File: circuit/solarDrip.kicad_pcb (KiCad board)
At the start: 2 copper layers, 57 x 50 mm, 41 parts, among them J1 solar_charger, J2 batt, J3 solar, J4 pump, J5 soil, J6 water, J7 USB_C_Receptacle_USB2.0_14P, J8 i2c, Q1 2N7002K, Q2 2N7002K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

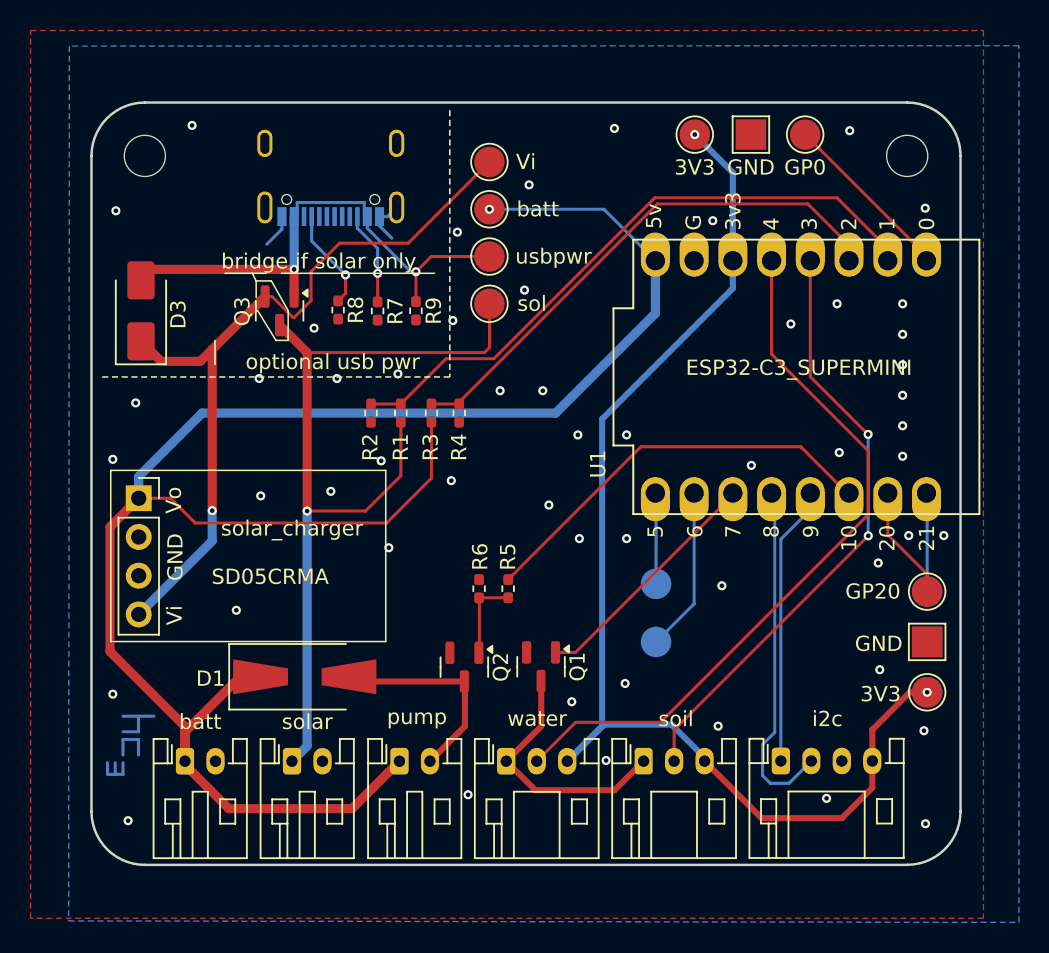
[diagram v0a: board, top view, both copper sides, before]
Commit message: flip usb and testpoint sides
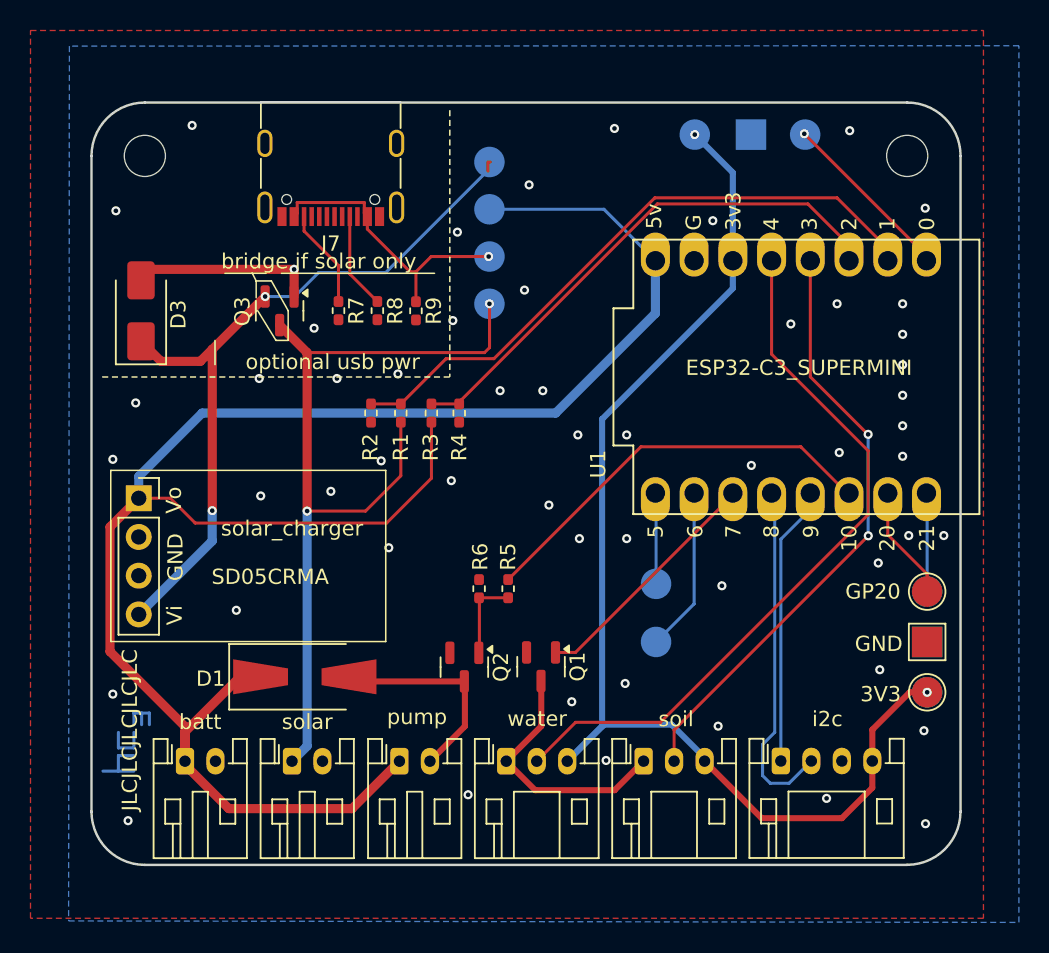
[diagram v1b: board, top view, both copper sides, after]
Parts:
- J7: moved to F.Cu
- TP1, TP10, TP15, TP2, TP3, TP6, TP7: moved to B.Cu
- moved REF** 4.92 mm to (21.5, 82.3), turned to 90 degrees
- moved R8 2.58 mm to (39.5, 52.1)
- moved R7 2.57 mm to (37.0, 52.1)
- turned J7 to 180 degrees
- turned TP1 to 180 degrees
- turned TP10 to 180 degrees
- turned TP15 to 180 degrees
- turned TP2 to 180 degrees
- turned TP3 to 180 degrees
- turned TP6 to 180 degrees
- turned TP7 to 180 degrees
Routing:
- net GND: track 5.36 -> 0.00 mm
- net vcc_usb: track 34.3 -> 30.9 mm
- net vcc_pwr: track 51.0 -> 49.1 mm, vias 1 -> 2
- net Net-(J7-CC2): track 6.15 -> 6.51 mm, vias 1 -> 0
- net Net-(J7-CC1): track 6.66 -> 6.32 mm, vias 1 -> 0
- net vcc_solar: track 55.4 -> 55.5 mm, vias 1 -> 2
- net gpio0: track 11.6 -> 11.7 mm, vias 0 -> 1
- net vcc_battery: vias 1 -> 0

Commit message: add capacitor, cleanup
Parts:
- removed REF**: muccc_logo, my_footprints:muccc_logo
- added C1: C_Polarized, Capacitor_THT:CP_Radial_D10.0mm_P7.50mm, F.Cu at (46.0, 71.0)
- moved R6 9.35 mm to (49.5, 61.6)
- moved R5 9.29 mm to (51.3, 61.6)
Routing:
- net vcc_battery: track 125.6 -> 138.9 mm
- net vcc_solar: track 55.5 -> 66.4 mm
- net Net-(Q2-G): track 5.54 -> 15.5 mm
- net out_pump: track 27.2 -> 20.4 mm
- net vcc_usb: track 30.9 -> 36.2 mm
- net out_sensors: track 16.0 -> 19.6 mm
- net GND: track 0.00 -> 2.74 mm, vias 54 -> 57
- net vcc_pwr: track 49.1 -> 51.7 mm
- net in-a_moisture: track 39.7 -> 42.2 mm
- net in-a_water: track 47.7 -> 49.6 mm
- net vcc_logic: vias 2 -> 1

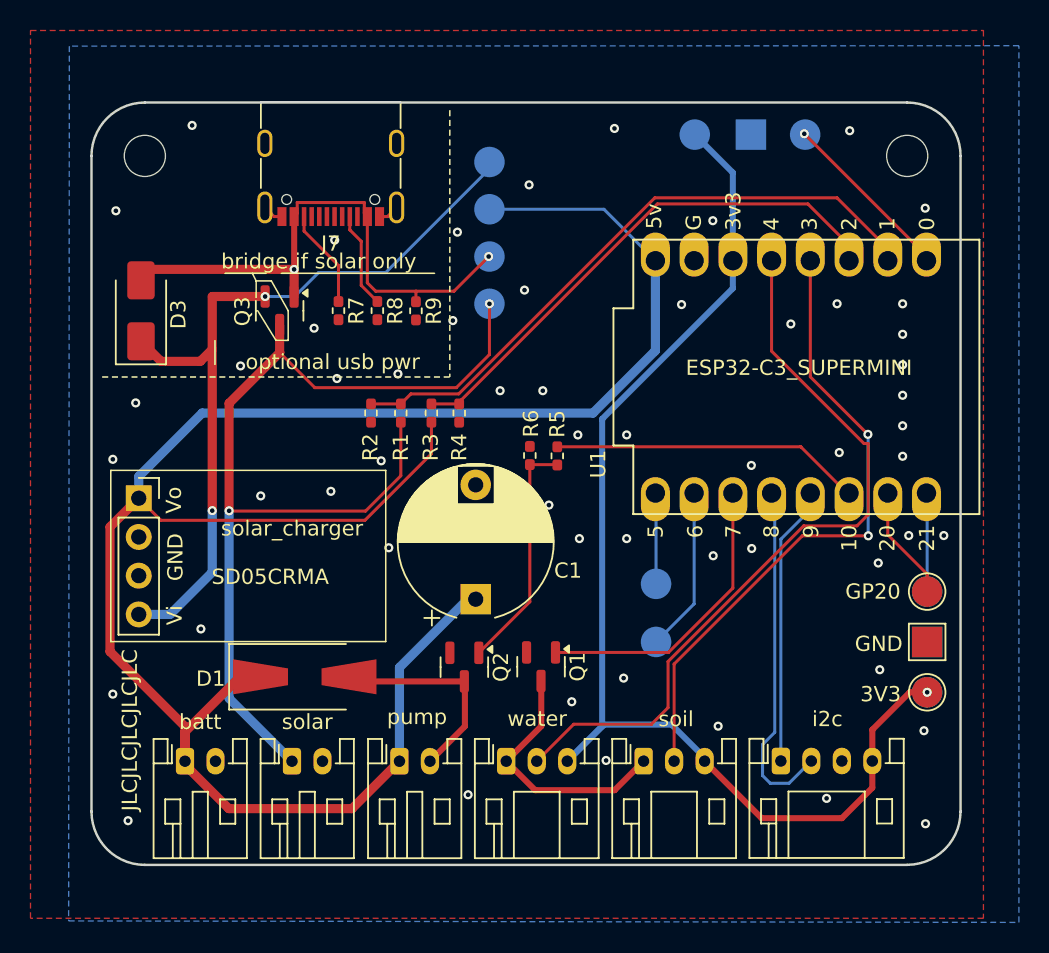
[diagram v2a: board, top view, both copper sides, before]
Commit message: move usb_pwr parts around
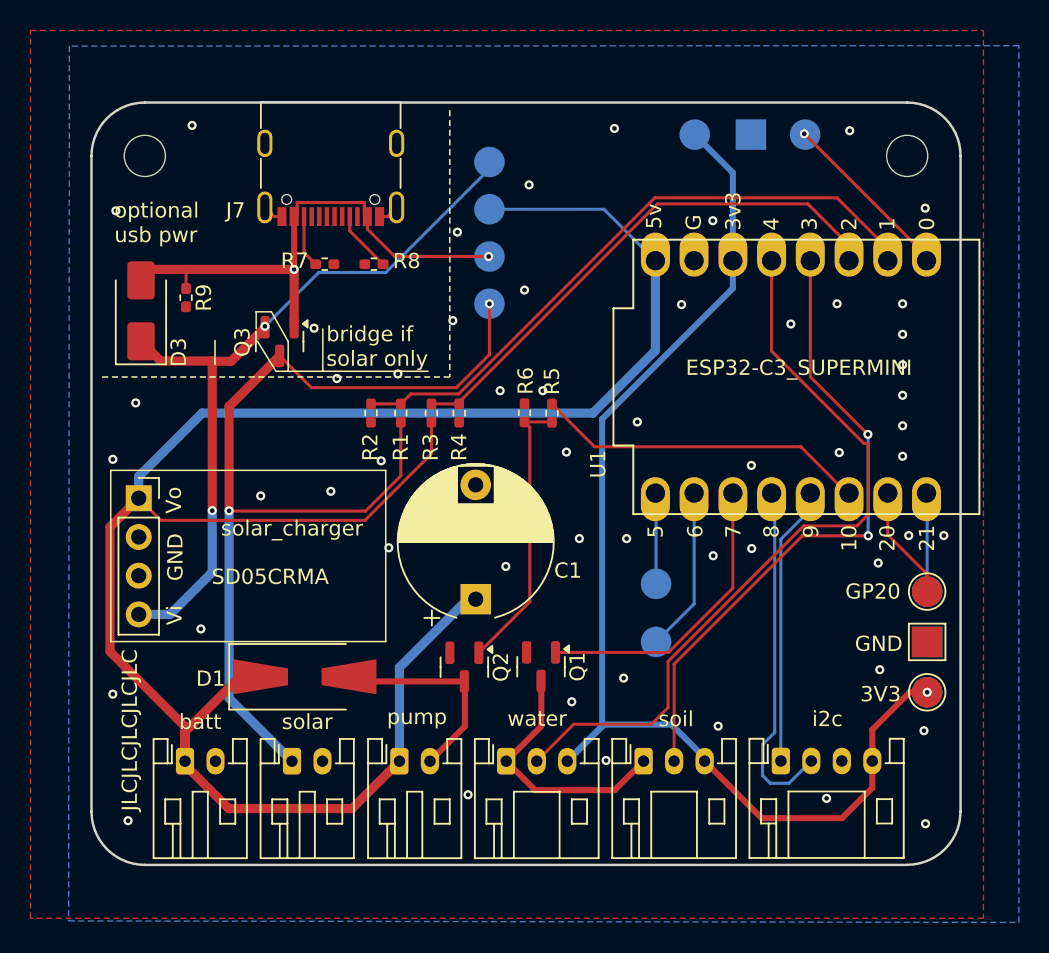
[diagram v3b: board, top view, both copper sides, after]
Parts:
- moved R9 15.1 mm to (26.9, 51.3)
- moved R7 3.18 mm to (36.0, 49.1), turned to 0 degrees
- moved R8 3.06 mm to (39.3, 49.1), turned to 180 degrees
- moved R6 2.82 mm to (49.1, 58.8)
- moved R5 2.82 mm to (51.0, 58.9)
- moved Q3 2.02 mm to (33.1, 54.1)
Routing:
- net Net-(J7-CC2): track 6.51 -> 3.43 mm
- net Net-(Q2-G): track 15.5 -> 18.5 mm
- net vcc_pwr: track 51.7 -> 48.9 mm
- net Net-(J7-CC1): track 6.32 -> 4.02 mm
- net vcc_solar: track 66.4 -> 64.3 mm
- net out_pump: track 20.4 -> 21.9 mm
- net vcc_usb: track 36.2 -> 34.9 mm
- net GND: vias 57 -> 55
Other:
- board text added: "SolarDripIrrigation v0.1 9R 05/2024"
- board text removed: "SolarDripIrigation v0.1 9R 05/2024"

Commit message: move more stuff around
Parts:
- C1: footprint Capacitor_THT:CP_Radial_D10.0mm_P7.50mm -> Capacitor_THT:CP_Radial_D8.0mm_P3.80mm
- moved J1 8.45 mm to (31.8, 61.4), turned to -90 degrees
- moved D1 4.54 mm to (37.0, 72.2), turned to -90 degrees
- moved C1 3.58 mm to (44.5, 67.8), turned to 0 degrees
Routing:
- net vcc_battery: track 138.9 -> 97.2 mm, vias 0 -> 2
- net vcc_pwr: track 48.9 -> 35.5 mm, vias 2 -> 1
- net vcc_solar: track 64.3 -> 51.5 mm, vias 2 -> 1
- net pump_low: track 13.9 -> 15.7 mm
- net GND: vias 55 -> 54
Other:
- board text added: "JLCJLCJLCJLC"
- board text removed: "JLCJLCJLCJLCJLC"

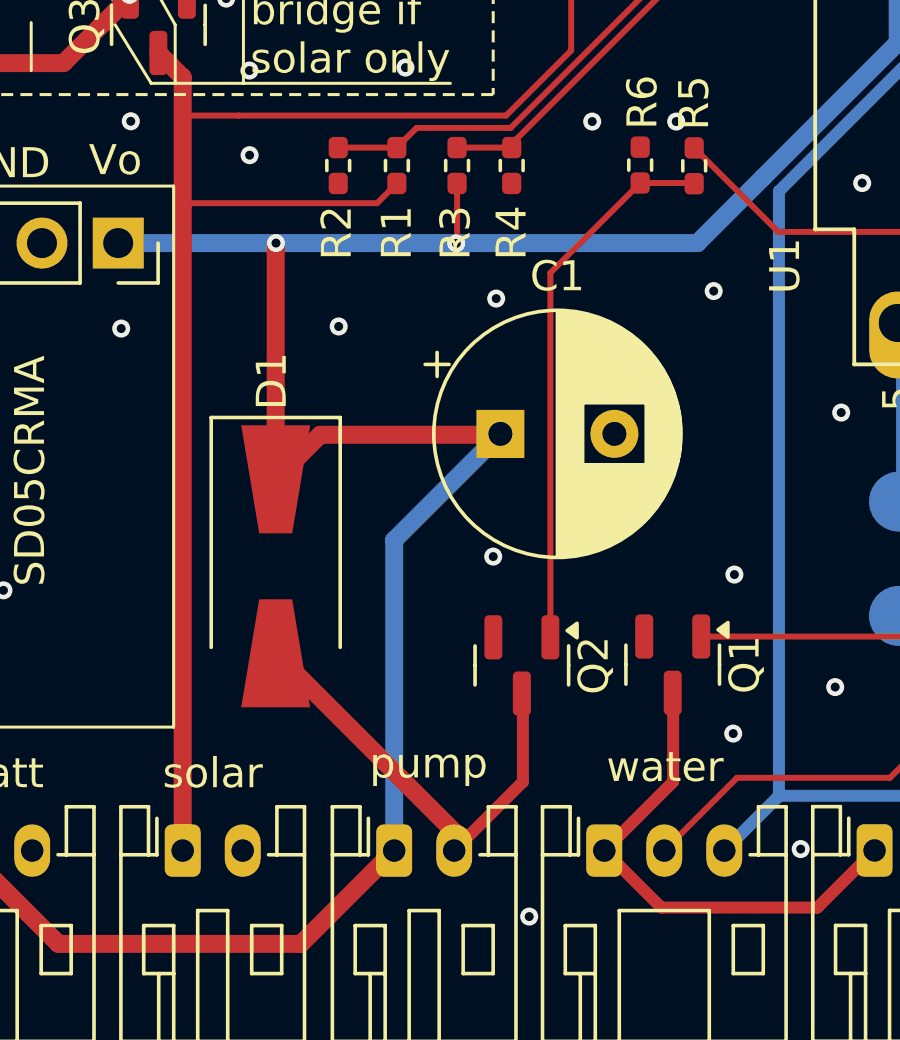
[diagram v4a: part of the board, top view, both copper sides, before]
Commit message: add motor cap
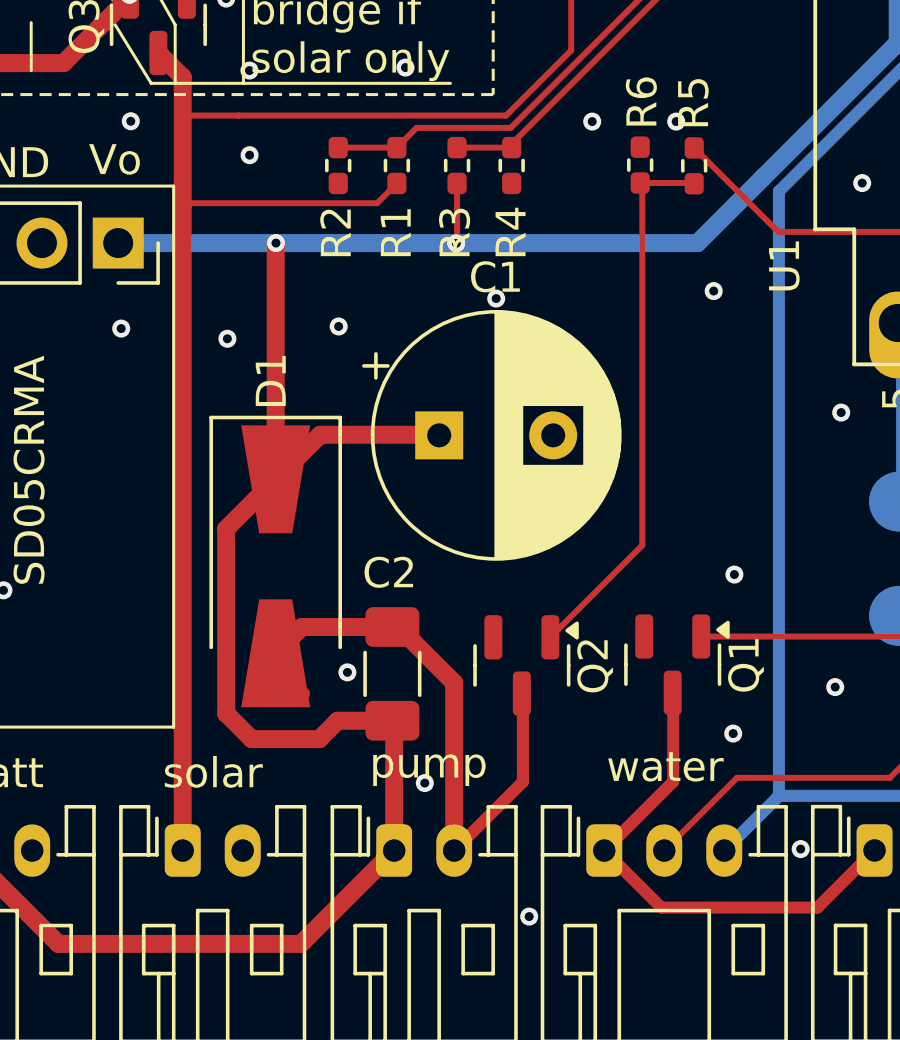
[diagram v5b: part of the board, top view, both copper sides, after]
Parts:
- added C2: C, Capacitor_SMD:C_1206_3216Metric_Pad1.33x1.80mm_HandSolder, F.Cu at (40.9, 75.8)
- moved C1 2.04 mm to (42.5, 67.8)
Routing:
- net pump_low: track 15.7 -> 19.4 mm
- net vcc_battery: track 97.2 -> 98.8 mm
- net GND: vias 54 -> 56

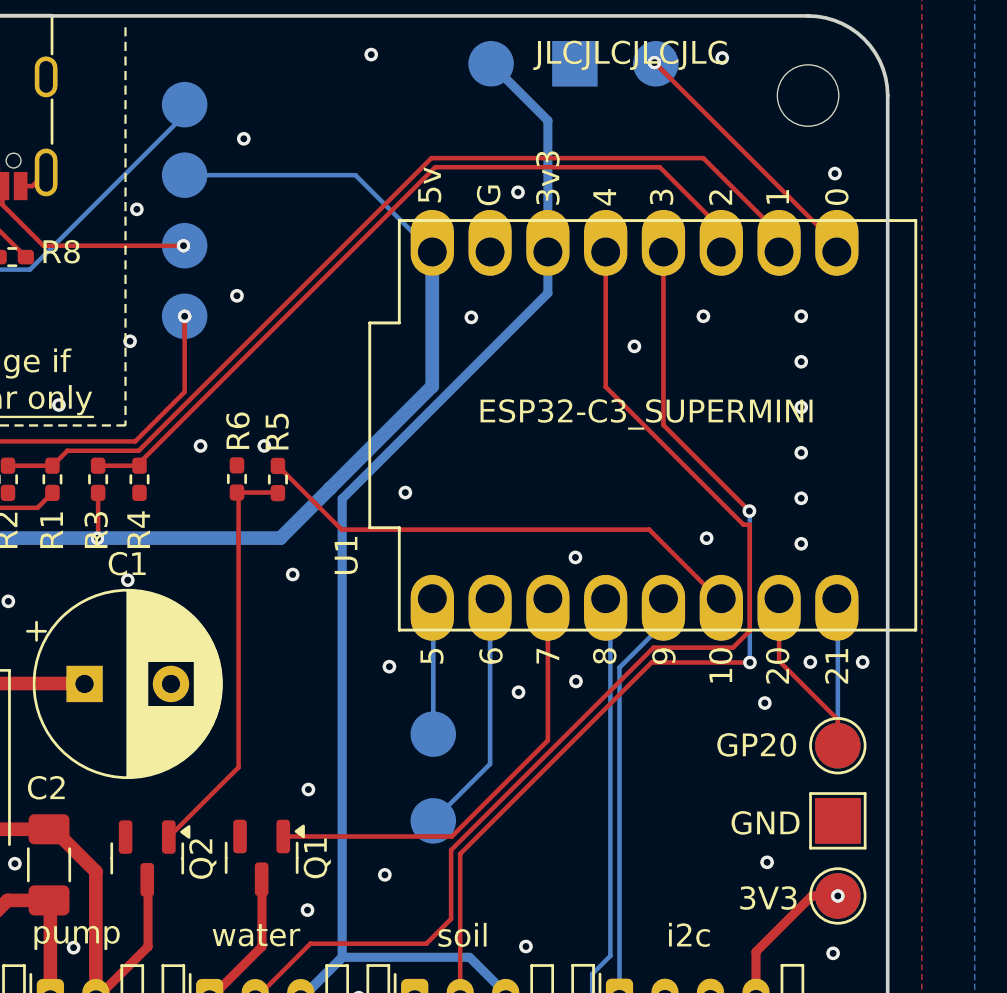
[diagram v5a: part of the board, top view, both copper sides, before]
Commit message: pcb: add U1 smd pads
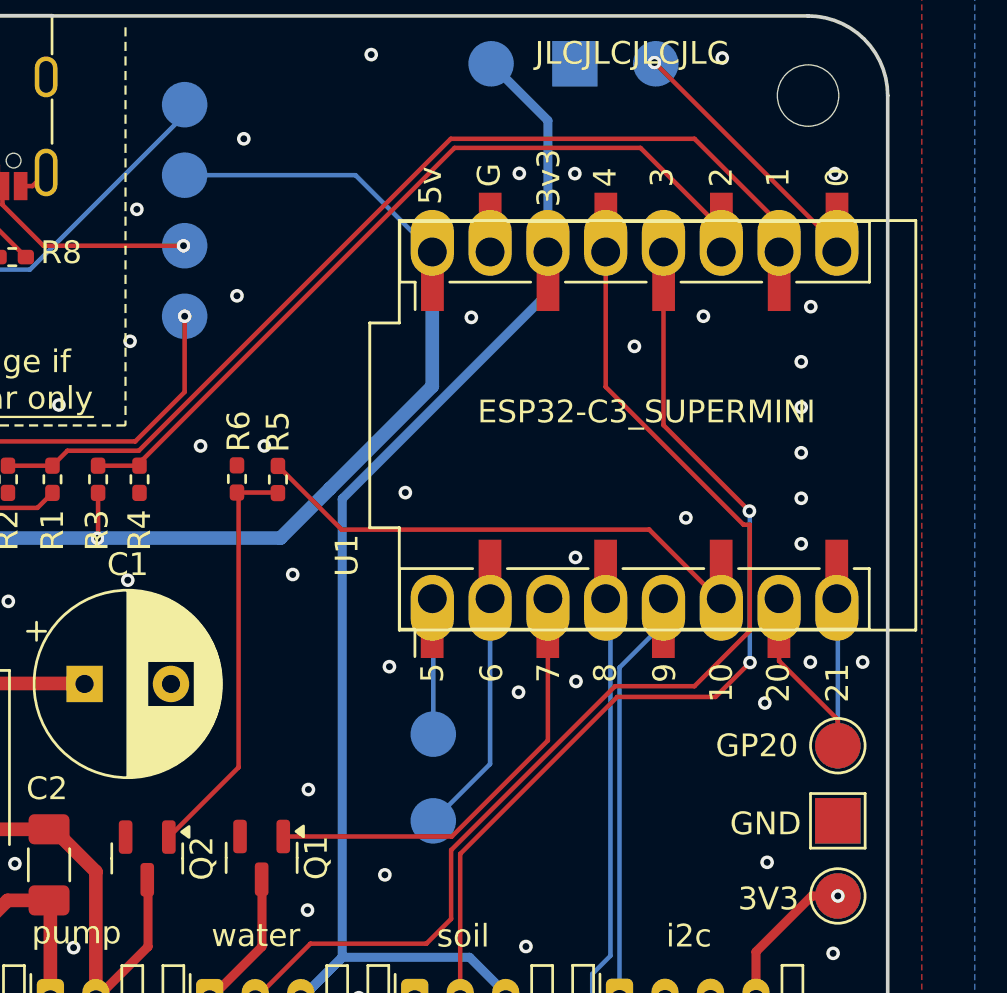
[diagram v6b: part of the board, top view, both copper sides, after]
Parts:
- added J10: Conn_01x08_Socket, Connector_PinSocket_2.54mm:PinSocket_1x08_P2.54mm_Vertical_SMD_Pin1Left, F.Cu at (66.6, 48.8)
- added J9: Conn_01x08_Socket, Connector_PinSocket_2.54mm:PinSocket_1x08_P2.54mm_Vertical_SMD_Pin1Left, F.Cu at (66.6, 64.1)
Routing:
- net GND: track 2.74 -> 4.39 mm, vias 56 -> 57
- net solar_hi: track 41.7 -> 42.6 mm
- net bat_hi: track 35.0 -> 35.7 mm
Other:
- board text added: "3V3"
- board text added: "SCL"
- board text added: "SDA"
